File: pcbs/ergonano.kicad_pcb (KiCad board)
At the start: 2 copper layers, 167.6 x 164.6 mm, 92 parts

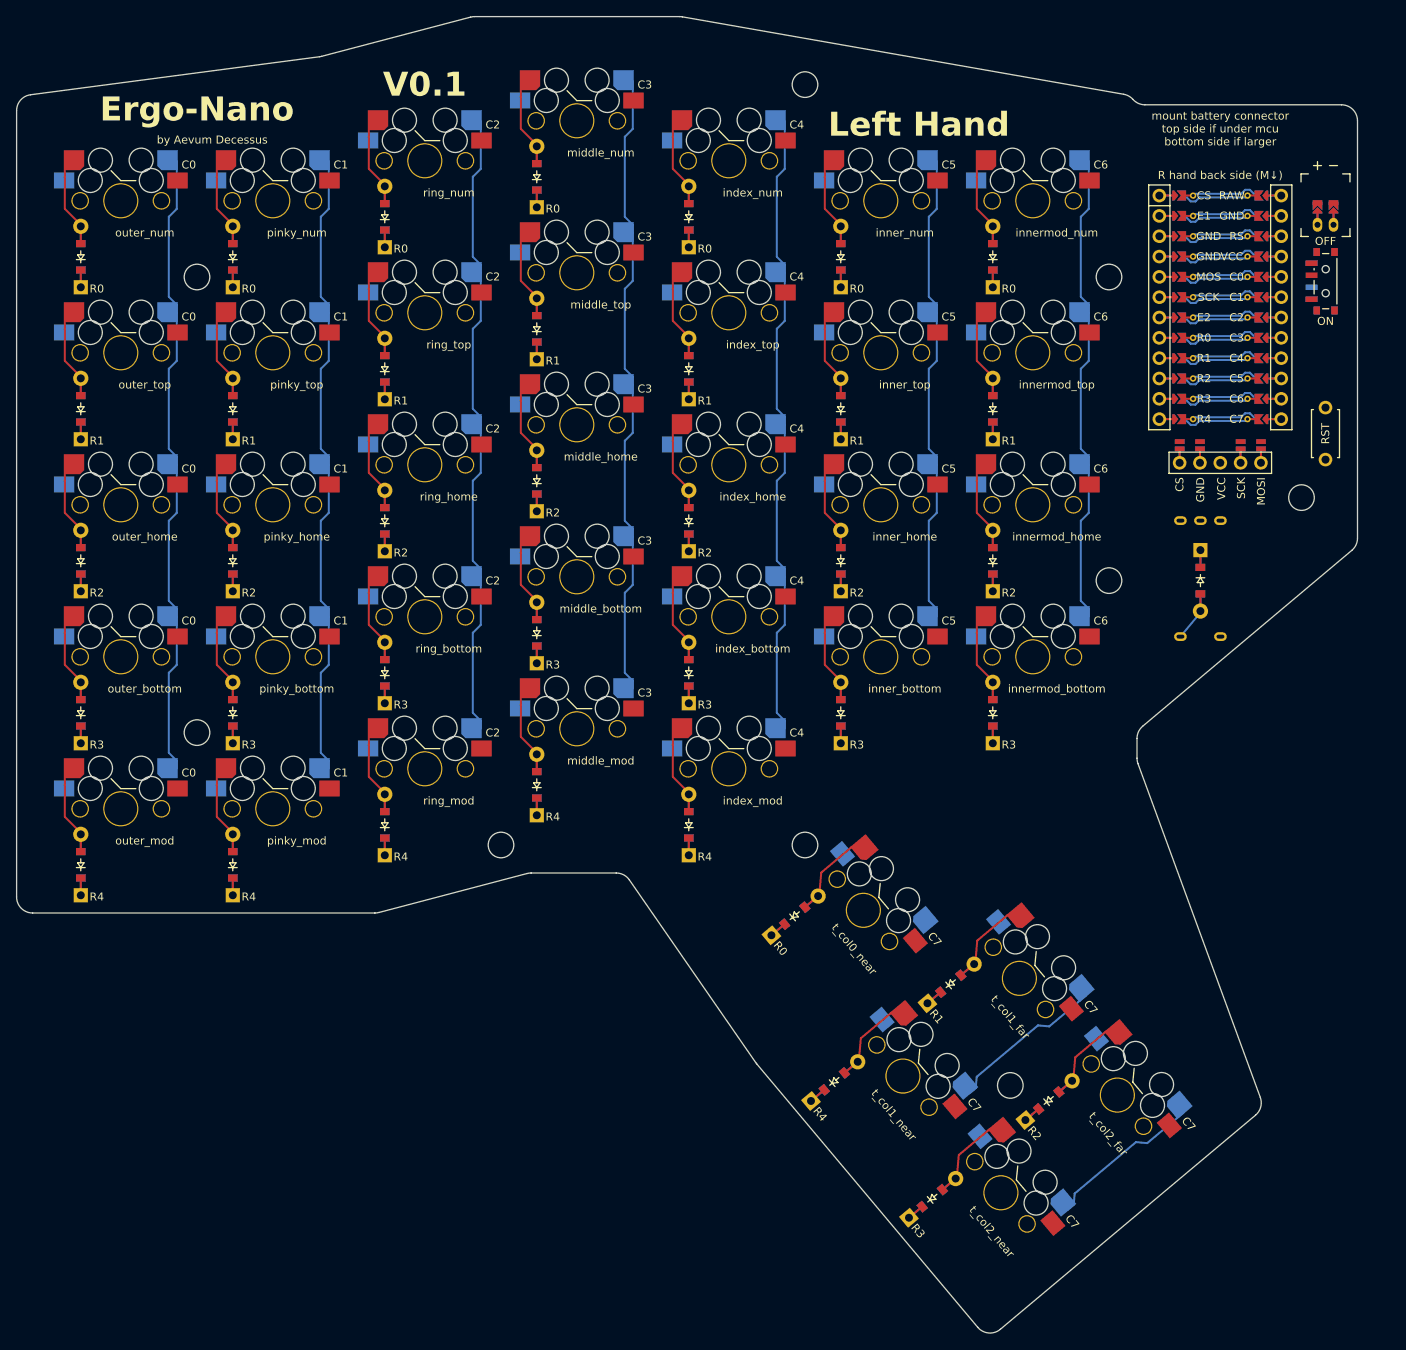
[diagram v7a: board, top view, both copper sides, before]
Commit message: Don't leave a pad at a 45 degree angle
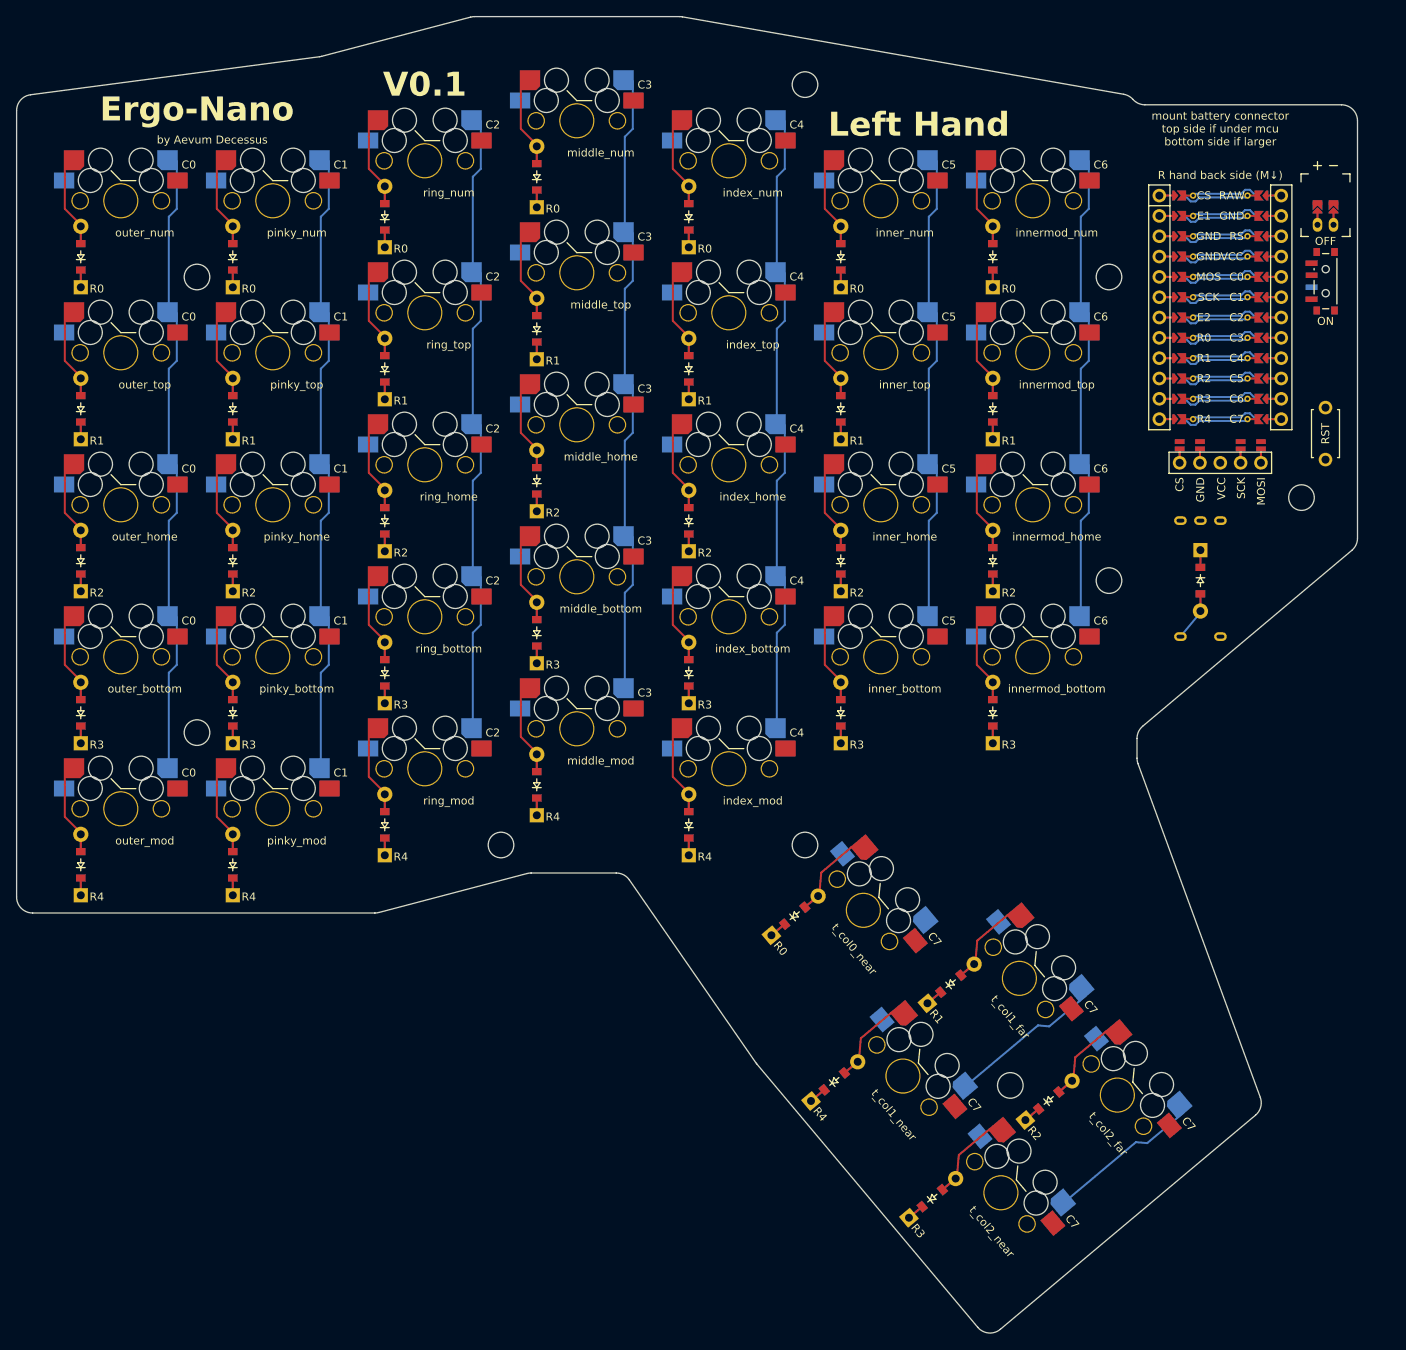
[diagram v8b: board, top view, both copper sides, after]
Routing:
- net (no net): track 904.5 -> 864.9 mm
